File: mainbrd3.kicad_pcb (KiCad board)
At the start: 4 copper layers, 100 x 72 mm, 110 parts, among them J1 Conn_01x04_Pin, J10 Conn_01x03_Pin, J2 USB_B_Micro, J3 Conn_01x02_Pin, J4 Conn_01x02_Pin, J5 https://abracon.com/Magnetics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, J6 Screw_Terminal_01x02, J7 Screw_Terminal_01x02, J8 Screw_Terminal_01x02, J9 Screw_Terminal_01x02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

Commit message: PCB Save: 2 files changed mainbrd3.kicad_pcb 12/0/1718 mainbrd3.kicad_prl 0/0/1
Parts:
- moved R21 23.0 mm to (176.1, 67.5)
- moved C28 9.00 mm to (189.0, 95.0)
- moved C10 8.77 mm to (161.5, 110.0)
- moved C11 8.77 mm to (155.1, 106.0)
- moved C12 8.77 mm to (155.1, 99.0)
- moved C13 8.77 mm to (150.5, 96.0)
- moved C3 8.77 mm to (171.5, 84.0)
- moved C34 8.77 mm to (159.5, 84.0)
- moved C4 8.77 mm to (181.1, 88.0)
- moved C5 8.77 mm to (181.1, 93.0)
- moved C6 8.77 mm to (181.1, 98.5)
- moved C7 8.77 mm to (181.1, 105.0)
- moved C8 8.77 mm to (173.5, 110.0)
- moved C9 8.77 mm to (167.5, 110.0)
- moved U1 8.71 mm to (168.0, 97.0)
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
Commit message: PCB Save: 1 files changed mainbrd3.kicad_pcb 437/0/814
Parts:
- R20, R21, R22: moved to B.Cu
- moved X1 109.9 mm to (186.4, 88.7), turned to 90 degrees
- moved R20 109.8 mm to (187.7, 68.6), turned to 90 degrees
- moved C29 109.1 mm to (188.5, 87.7), turned to -90 degrees
- moved R21 13.9 mm to (190.0, 67.9), turned to -90 degrees
- moved R22 11.8 mm to (187.7, 66.5), turned to 90 degrees
- moved C28 4.63 mm to (188.5, 90.4), turned to -90 degrees
- moved U3 3.94 mm to (192.9, 88.3)
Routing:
- net Net-(U3-LED2/~{INTSEL}): track 0.00 -> 52.3 mm, vias 0 -> 1
- net Net-(U3-LED1/REGOFF): track 0.00 -> 36.7 mm, vias 0 -> 1
- net Net-(J5-Pad14): track 0.00 -> 8.38 mm
- net Net-(U3-XTAL1/CLKIN): track 0.00 -> 5.86 mm
- net GND: track 43.2 -> 48.0 mm, vias 41 -> 44
- net Net-(U3-XTAL2): track 0.00 -> 4.02 mm
- net Net-(J5-Pad12): track 0.00 -> 3.02 mm

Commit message: PCB Save: 3 files changed mainbrd3.kicad_pcb 3388/0/1892 mainbrd3.kicad_prl 0/0/2 mainbrd3.kicad_pro 0/0/3
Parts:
- R18: moved to B.Cu
- moved L2 124.4 mm to (199.2, 81.2), turned to -90 degrees
- moved R16 119.1 mm to (197.5, 95.7)
- moved R10 118.8 mm to (194.3, 102.0), turned to 90 degrees
- moved R19 116.3 mm to (197.5, 96.9)
- moved C31 113.2 mm to (177.7, 80.0), turned to 90 degrees
- moved R17 112.2 mm to (190.6, 97.6)
- moved R18 98.8 mm to (176.9, 111.9)
- moved J6 23.4 mm to (127.5, 64.0)
- moved R21 16.0 mm to (174.0, 67.8), turned to 180 degrees
- moved R22 14.1 mm to (174.0, 69.9), turned to 0 degrees
- moved R20 13.7 mm to (174.0, 68.9), turned to 180 degrees
- moved C29 2.64 mm to (186.2, 86.4), turned to 0 degrees
- moved C28 2.31 mm to (186.2, 90.0), turned to 0 degrees
- moved X1 0.54 mm to (186.2, 88.2)
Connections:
- J2 pad SH: (no net) -> Earth
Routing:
- net NRST: track 0.00 -> 51.9 mm, vias 0 -> 2
- net Net-(U3-~{INT}/REFCLKO): track 0.00 -> 40.2 mm, vias 0 -> 3
- net ETH_MDC: track 0.00 -> 40.1 mm, vias 0 -> 2
- net Earth: track 0.00 -> 37.5 mm
- net ETH_TXD1: track 0.00 -> 37.1 mm, vias 0 -> 2
- net ETH_MDIO: track 0.00 -> 35.3 mm, vias 0 -> 3
- net ETH_TXD0: track 0.00 -> 34.9 mm, vias 0 -> 2
- net ETH_TX_EN: track 0.00 -> 30.3 mm, vias 0 -> 2
- net D+: track 0.00 -> 25.0 mm
- net D-: track 0.05 -> 25.0 mm
- net Net-(J5-Pad12): track 3.02 -> 19.6 mm
- net Net-(U3-RXER/PHYAD0): track 0.00 -> 12.2 mm, vias 0 -> 2
- net Net-(U3-LED1/REGOFF): track 36.7 -> 48.7 mm, vias 1 -> 2
- net Net-(U3-LED2/~{INTSEL}): track 52.3 -> 40.3 mm
- net Net-(C31-Pad1): track 0.00 -> 9.48 mm
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- added copper zone on F.Cu, net +3V3_ethtxrx
- added copper zone on In2.Cu, net +3V3_ethtxrx
- added copper zone on B.Cu, net GND
- added copper zone on F.Cu, net Net-(U3-XTAL1/CLKIN)
- added copper zone on F.Cu, net Net-(U3-XTAL2)

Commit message: PCB Save: 1 files changed mainbrd3.kicad_pcb 1419/0/1758
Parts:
- moved R7 119.5 mm to (194.4, 83.3), turned to 180 degrees
- moved R14 119.1 mm to (197.5, 98.3)
- moved R15 119.0 mm to (197.5, 99.4)
- moved R6 117.3 mm to (192.4, 83.3)
- moved R9 115.0 mm to (189.2, 82.4), turned to -90 degrees
- moved R8 114.5 mm to (189.2, 84.4), turned to 90 degrees
- moved R11 107.0 mm to (182.5, 102.4)
- moved R13 106.5 mm to (184.5, 103.5)
- moved R12 104.4 mm to (182.5, 101.3)
- moved R17 0.10 mm to (190.6, 97.5)
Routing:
- net Net-(U3-RXD0/MODE0): track 0.00 -> 25.1 mm, vias 0 -> 3
- net Net-(U3-RXD1/MODE1): track 0.00 -> 25.0 mm, vias 0 -> 2
- net Net-(U3-CRS_DV/MODE2): track 7.62 -> 26.7 mm, vias 2 -> 3
- net /ETH/Erx-: track 0.00 -> 18.2 mm, vias 0 -> 1
- net /ETH/Erx+: track 0.00 -> 16.0 mm, vias 0 -> 1
- net /ETH/Etx-: track 0.00 -> 13.4 mm
- net /ETH/Etx+: track 0.00 -> 12.2 mm
- net ETH_CRS_DV: track 0.00 -> 5.65 mm
- net Net-(U3-~{INT}/REFCLKO): track 40.2 -> 45.0 mm, vias 3 -> 4
- net ETH_RXD1: track 0.00 -> 3.50 mm
- net ETH_RXD0: track 0.00 -> 3.38 mm
- net +3V3_ethtxrx: vias 8 -> 13

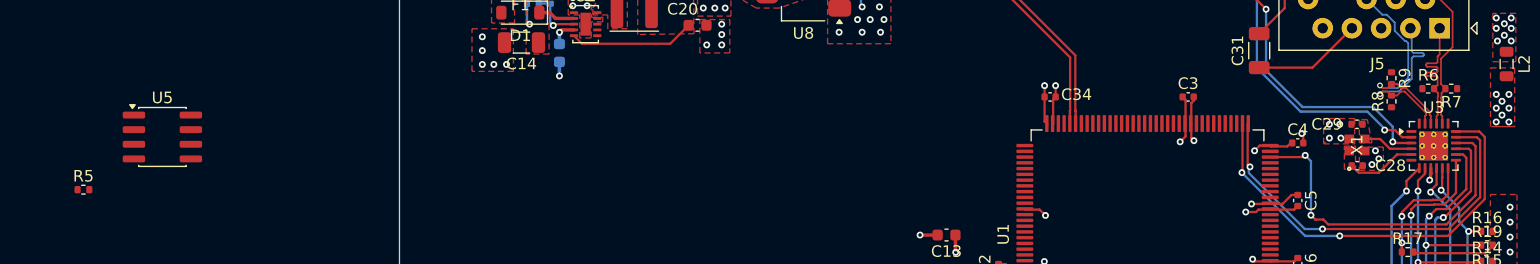
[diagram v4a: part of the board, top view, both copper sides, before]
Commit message: PCB Save: 1 files changed mainbrd3.kicad_pcb 500/0/531
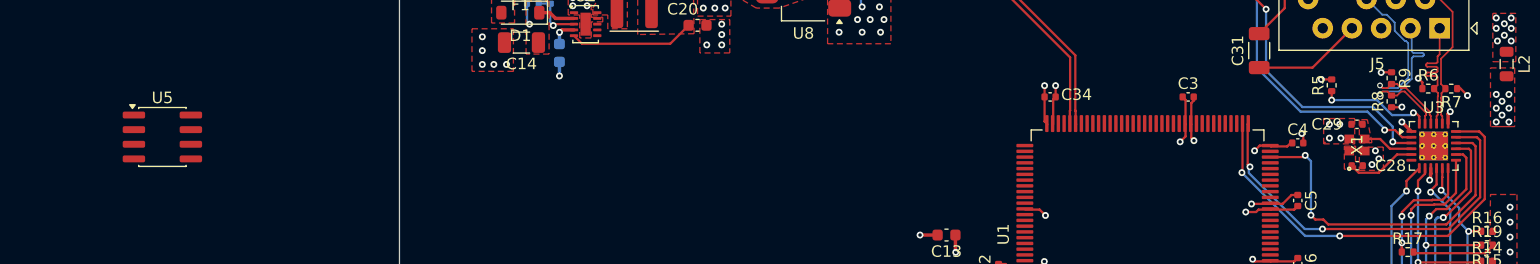
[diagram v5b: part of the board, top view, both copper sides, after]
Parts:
- moved R5 108.8 mm to (184.0, 83.0), turned to 90 degrees
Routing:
- net Net-(U3-RBIAS): track 0.00 -> 9.77 mm, vias 0 -> 2
- net +3V3_ethtxrx: track 7.19 -> 13.5 mm, vias 13 -> 19
- net GND: track 44.1 -> 45.0 mm, vias 52 -> 53
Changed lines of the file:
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@@
 	(footprint "Resistor_SMD:R_0402_1005Metric"
 		(layer "F.Cu")
-		(at 75.54 92.08)
+		(at 184 83.01 90)
 		(descr "Resistor SMD 0402 (1005 Metric), square (rectangular) end terminal, IPC-7351 nominal, (Body size source: IPC-SM-782 page 72, https://www.pcb-3d.com/wordpress/wp-content/uploads/ipc-sm-782a_amendment_1_and_2.pdf)")
 		(tags "resistor")
 		(property "Reference" "R5"
-			(at 0 -1.17 0)
+			(at 0 -1.17 90)
 			(layer "F.SilkS")
 			(effects
@@
 		)
 		(property "Value" "12K1"
-			(at 0 1.17 0)
+			(at 0 1.17 90)
 			(layer "F.Fab")
 			(effects
@@
 		)
 		(property "Datasheet" "https://www.lcsc.com/datasheet/lcsc_datasheet_2206010045_UNI-ROYAL-Uniroyal-Elec-0402WGF1212TCE_C25852.pdf"
-			(at 0 0 0)
+			(at 0 0 90)
 			(layer "F.Fab")
 			(hide yes)
@@
 		)
 		(property "Description" "0402WGF1212TCE"
-			(at 0 0 0)
+			(at 0 0 90)
 			(layer "F.Fab")
 			(hide yes)
@@
 		)
 		(property "KiLib_Generator" "SMD_2terminal_chip_molded"
-			(at 0 0 0)
+			(at 0 0 90)
 			(layer "F.SilkS")
 			(hide yes)
@@
 		)
 		(property "JLCPCB PN" "C25852"
-			(at 0 0 0)
+			(at 0 0 90)
 			(unlocked yes)
 			(layer "F.Fab")
@@
 		)
 		(fp_text user "${REFERENCE}"
-			(at 0 0 0)
+			(at 0 0 90)
 			(layer "F.Fab")
 			(effects
@@
 		)
 		(pad "1" smd roundrect
-			(at -0.51 0)
+			(at -0.51 0 90)
 			(size 0.54 0.64)
 			(layers "F.Cu" "F.Mask" "F.Paste")
@@
 		)
 		(pad "2" smd roundrect
-			(at 0.51 0)
+			(at 0.51 0 90)
 			(size 0.54 0.64)
 			(layers "F.Cu" "F.Mask" "F.Paste")
@@
 	)
 	(segment
+		(start 184 82.5)
+		(end 183.1 82.5)
+		(width 0.2)
+		(layer "F.Cu")
+		(net "GND")
+	)
+	(segment
 		(start 181.0525 93.5025)
 		(end 180.7425 93.8125)
@@
 	)
 	(via
+		(at 183.1 82.5)
+		(size 0.6)
+		(drill 0.3)
+		(layers "F.Cu" "B.Cu")
+		(net "GND")
+	)
+	(via
 		(at 181.4 87.2)
 		(size 0.6)
@@
 	)
 	(segment
+		(start 189.2 81.88)
+		(end 188.32 81.88)
+		(width 0.2)
+		(layer "F.Cu")
+		(net "+3V3_ethtxrx")
+	)
+	(segment
 		(start 191.11 97.6)
 		(end 197.31 97.6)
@@
 	)
 	(segment
+		(start 194.9 83.3)
+		(end 195.2 83.3)
+		(width 0.2)
+		(layer "F.Cu")
+		(net "+3V3_ethtxrx")
+	)
+	(segment
+		(start 190.925 87.025)
+		(end 190.1 86.2)
+		(width 0.3)
+		(layer "F.Cu")
+		(net "+3V3_ethtxrx")
+	)
+	(segment
+		(start 190.08 84.92)
+		(end 190.1 84.9)
+		(width 0.2)
+		(layer "F.Cu")
+		(net "+3V3_ethtxrx")
+	)
+	(segment
 		(start 197.31 97.6)
 		(end 198.01 96.9)
@@
 		(net "+3V3_ethtxrx")
 	)
+	(segment
+		(start 195.2 83.3)
+		(end 195.8 83.9)
+		(width 0.2)
+		(layer "F.Cu")
+		(net "+3V3_ethtxrx")
+	)
+	(segment
+		(start 194.1125 86.3375)
+		(end 194.1125 85.4875)
+		(width 0.3)
+		(layer "F.Cu")
+		(net "+3V3_ethtxrx")
+	)
+	(segment
+		(start 188.32 81.88)
+		(end 188.3 81.9)
+		(width 0.2)
+		(layer "F.Cu")
+		(net "+3V3_ethtxrx")
+	)
+	(segment
+		(start 191.88 83.3)
+		(end 191.88 82.755)
+		(width 0.2)
+		(layer "F.Cu")
+		(net "+3V3_ethtxrx")
+	)
+	(segment
+		(start 189.2 84.92)
+		(end 190.08 84.92)
+		(width 0.2)
+		(layer "F.Cu")
+		(net "+3V3_ethtxrx")
+	)
+	(segment
+		(start 194.1125 85.4875)
+		(end 194.3 85.3)
+		(width 0.3)
+		(layer "F.Cu")
+		(net "+3V3_ethtxrx")
+	)
+	(segment
+		(start 191.88 82.755)
+		(end 191.525 82.4)
+		(width 0.2)
+		(layer "F.Cu")
+		(net "+3V3_ethtxrx")
+	)
 	(via
 		(at 199.4 85)
@@
 	)
 	(via
+		(at 191.525 82.4)
+		(size 0.6)
+		(drill 0.3)
+		(layers "F.Cu" "B.Cu")
+		(net "+3V3_ethtxrx")
+	)
+	(via
 		(at 199.5 93.6)
 		(size 0.6)
@@
 	)
 	(via
+		(at 195.8 83.9)
+		(size 0.6)
+		(drill 0.3)
+		(layers "F.Cu" "B.Cu")
+		(net "+3V3_ethtxrx")
+	)
+	(via
+		(at 190.1 86.2)
+		(size 0.6)
+		(drill 0.3)
+		(layers "F.Cu" "B.Cu")
+		(net "+3V3_ethtxrx")
+	)
+	(via
+		(at 188.3 81.9)
+		(size 0.6)
+		(drill 0.3)
+		(layers "F.Cu" "B.Cu")
+		(net "+3V3_ethtxrx")
+	)
+	(via
+		(at 190.1 84.9)
+		(size 0.6)
+		(drill 0.3)
+		(layers "F.Cu" "B.Cu")
+		(net "+3V3_ethtxrx")
+	)
+	(via
 		(at 199.5 94.9)
 		(size 0.6)
@@
 		(net "+3V3_ethtxrx")
 	)
+	(via
+		(at 194.3 85.3)
+		(size 0.6)
+		(drill 0.3)
+		(layers "F.Cu" "B.Cu")
+		(net "+3V3_ethtxrx")
+	)
 	(segment
 		(start 192.2 81.2)
@@
 	)
 	(segment
+		(start 191.3 85.4)
+		(end 191.6125 85.7125)
+		(width 0.2)
+		(layer "F.Cu")
+		(net "Net-(U3-RBIAS)")
+	)
+	(segment
+		(start 191.6125 85.7125)
+		(end 191.6125 86.3375)
+		(width 0.2)
+		(layer "F.Cu")
+		(net "Net-(U3-RBIAS)")
+	)
+	(segment
+		(start 191.1 85.4)
+		(end 191.3 85.4)
+		(width 0.2)
+		(layer "F.Cu")
+		(net "Net-(U3-RBIAS)")
+	)
+	(segment
+		(start 184 84.3)
+		(end 184 83.52)
+		(width 0.2)
+		(layer "F.Cu")
+		(net "Net-(U3-RBIAS)")
+	)
+	(via
+		(at 191.1 85.4)
+		(size 0.6)
+		(drill 0.3)
+		(layers "F.Cu" "B.Cu")
+		(net "Net-(U3-RBIAS)")
+	)
+	(via
+		(at 184 84.3)
+		(size 0.6)
+		(drill 0.3)
+		(layers "F.Cu" "B.Cu")
+		(net "Net-(U3-RBIAS)")
+	)
+	(segment
+		(start 189.244123 85.6)
+		(end 187.944123 84.3)
+		(width 0.2)
+		(layer "B.Cu")
+		(net "Net-(U3-RBIAS)")
+	)
+	(segment
+		(start 190.9 85.6)
+		(end 189.244123 85.6)
+		(width 0.2)
+		(layer "B.Cu")
+		(net "Net-(U3-RBIAS)")
+	)
+	(segment
+		(start 187.944123 84.3)
+		(end 184 84.3)
+		(width 0.2)
+		(layer "B.Cu")
+		(net "Net-(U3-RBIAS)")
+	)
+	(segment
+		(start 191.1 85.4)
+		(end 190.9 85.6)
+		(width 0.2)
+		(layer "B.Cu")
+		(net "Net-(U3-RBIAS)")
+	)
+	(segment
 		(start 192.6 92.150454)
 		(end 193.1125 91.637954)
@@
 		(polygon
 			(pts
-				(xy 190.5 81.5) (xy 200.026182 81.5) (xy 200.071257 100.197176) (xy 197.778873 100.202703) (xy 197.85 87.4)
-				(xy 197.094741 86.636365) (xy 190.5 86.6)
+				(xy 187.7 81.5) (xy 200.026182 81.5) (xy 200.071257 100.197176) (xy 197.778873 100.202703) (xy 197.85 87.4)
+				(xy 197.094741 86.636365) (xy 187.7 86.58456)
 			)
 		)

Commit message: PCB Save: 2 files changed mainbrd3.kicad_pcb 351/0/833 mainbrd3.kicad_prl 0/0/1
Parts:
- C27, U4: moved to B.Cu
- moved C27 116.7 mm to (187.1, 67.6), turned to 180 degrees
- moved U4 114.9 mm to (187.8, 70.0), turned to 180 degrees
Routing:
- net +3V3_ethtxrx: track 13.5 -> 43.9 mm, vias 19 -> 20
- net /ETH/Etx+: track 12.2 -> 23.9 mm
- net /ETH/Erx+: track 16.0 -> 25.8 mm
- net /ETH/Erx-: track 18.2 -> 27.1 mm
- net /ETH/Etx-: track 13.4 -> 19.3 mm
- net GND: track 45.0 -> 47.6 mm, vias 53 -> 55

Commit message: PCB Save: 2 files changed mainbrd3.kicad_pcb 2103/0/7861 mainbrd3.kicad_prl 0/0/2
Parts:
- D3, D4: moved to B.Cu
- moved R23 123.7 mm to (154.3, 102.6)
- moved R24 122.3 mm to (154.3, 101.5)
- moved U7 120.7 mm to (189.4, 118.4), turned to -90 degrees
- moved R28 119.5 mm to (164.8, 71.2), turned to 90 degrees
- moved J8 119.1 mm to (174.6, 127.0)
- moved R25 118.7 mm to (160.3, 76.6)
- moved D4 118.1 mm to (189.4, 121.3), turned to 90 degrees
- moved R26 118.0 mm to (160.3, 75.4)
- moved R39 117.6 mm to (190.5, 123.8)
- moved R27 117.2 mm to (160.3, 77.8)
- moved R38 116.6 mm to (188.2, 123.8)
- moved R40 116.2 mm to (189.3, 125.0)
- moved J7 113.4 mm to (159.7, 126.9)
- moved R35 113.3 mm to (185.1, 119.2)
- moved R36 112.0 mm to (185.1, 118.2)
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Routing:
- net I2C1_SDA: track 0.00 -> 37.0 mm, vias 0 -> 2
- net I2C1_SCL: track 0.00 -> 35.6 mm, vias 0 -> 2
- net +3V3: track 41.6 -> 59.9 mm, vias 31 -> 40
- net GND: track 47.6 -> 61.3 mm, vias 55 -> 60
- net UART5_RX: track 0.00 -> 7.88 mm
- net UART4_RX: track 0.00 -> 7.72 mm
- net Net-(U5-A2): track 0.00 -> 7.01 mm
- net Net-(D3-A2): track 0.00 -> 6.98 mm, vias 0 -> 1
- net Net-(D4-A1): track 0.00 -> 6.95 mm, vias 0 -> 1
- net Net-(D4-A2): track 0.00 -> 6.94 mm, vias 0 -> 1
- net Net-(D3-A1): track 0.00 -> 6.86 mm, vias 0 -> 1
- net UART5_DIR: track 0.00 -> 5.96 mm
- net UART4_DIR: track 0.00 -> 5.89 mm
- net Net-(U5-A1): track 0.00 -> 5.25 mm
- net UART4_TX: track 0.00 -> 3.44 mm
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
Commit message: PCB Save: 2 files changed mainbrd3.kicad_pcb 0/1115/2443 mainbrd3.kicad_prl 0/0/1
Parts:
- moved R6 1.93 mm to (194.3, 83.1)
- moved R7 1.93 mm to (196.3, 83.1)
- moved R8 1.71 mm to (190.8, 83.8)
- moved R9 1.71 mm to (190.8, 81.8)
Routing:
- net +3V3_ethtxrx: track 43.9 -> 29.4 mm, vias 20 -> 6
- net /ETH/Etx+: track 23.9 -> 24.6 mm
- net /ETH/Etx-: track 19.3 -> 20.0 mm
- net +3V3: vias 40 -> 37
- removed copper zone on In2.Cu, net +3V3_ethtxrx
